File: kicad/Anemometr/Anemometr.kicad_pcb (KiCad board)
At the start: 2 copper layers, 44.9 x 48.9 mm, 158 parts, among them J1 Conn_01x01_Female, J10 +Z3, J11 -Z3, J12 +Z4, J13 -Z4, J14 SWD, J15 SWC, J16 Z4, J17 Z4, J18 1, J19 2, J2 Conn_01x01_Female, J20 3, J21 4, J22 5, J23 6, J24 7, J25 8, J26 Z4, J27 Z4, J28 Z4, J29 Z4, J3 RST, J30 Z4, J31 Z4, J32 Z4, J33 Z4, J34 Z4, J35 Z4, J4 TxD, J5 RxD, J6 +Z1, J7 -Z1, J8 +Z2, J9 -Z2, U1 TS5A3166DBVR, U10 MCP1700-3002E, U2 LMV7239, U3 TS5A3166DBVR, U4 TS5A3166DBVR, U5 STM32F103C8Tx, U6 TS5A3166DBVR, U7 LM2734Y, U8 MCP1700-5002E, U9 MCP1700-3002E, Y1 8MHz, Y2 25MHz

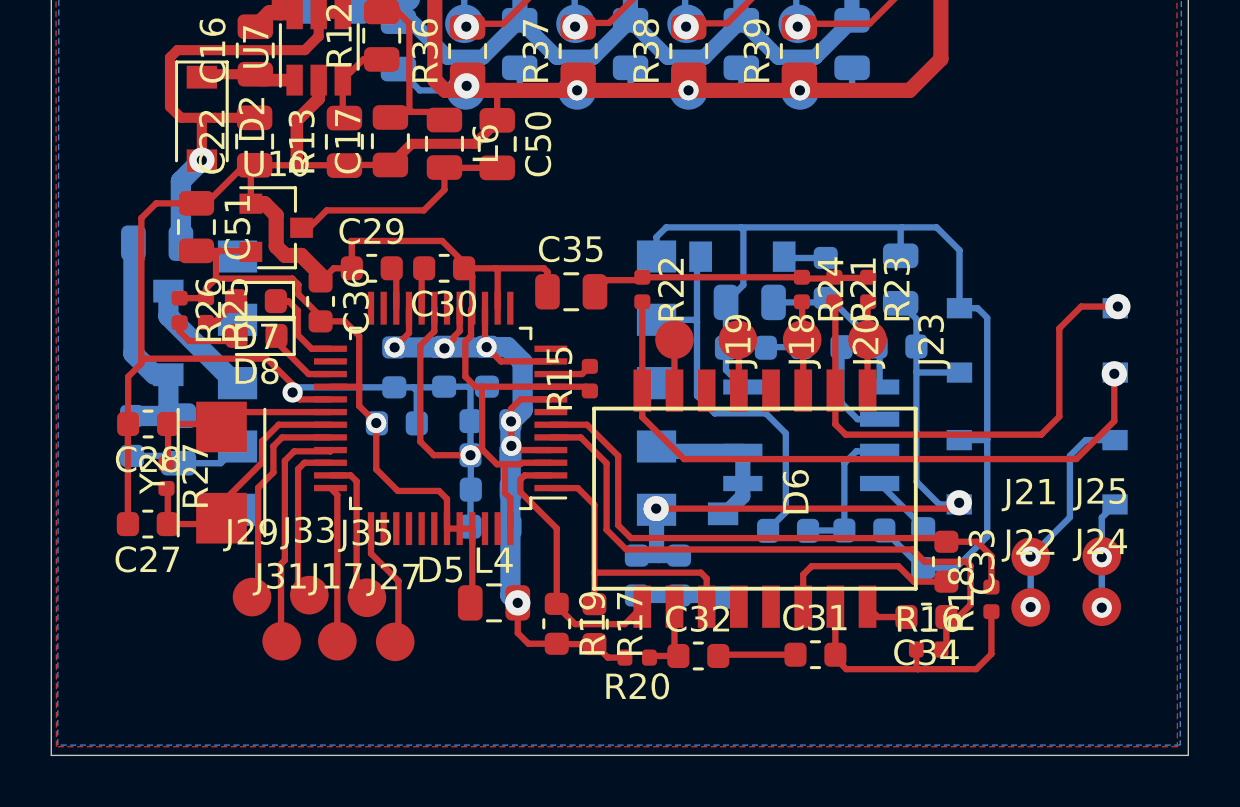
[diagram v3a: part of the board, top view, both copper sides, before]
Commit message: изменено:      kicad/Anemometr/Anemometr-cache.lib 	изменено:      kicad/Anemometr/Anemometr-rescue.lib 	изменено:      kicad/Anemometr/Anemometr.kicad_pcb 	изменено:      kicad/Anemometr/Anemometr.kicad_pcb-bak 	изменено:      kicad/Anemometr/Anemometr.sch 	изменено:      kicad/Anemometr/Anemometr.sch-bak 	изменено:      kicad/Anemometr/fp-info-cache
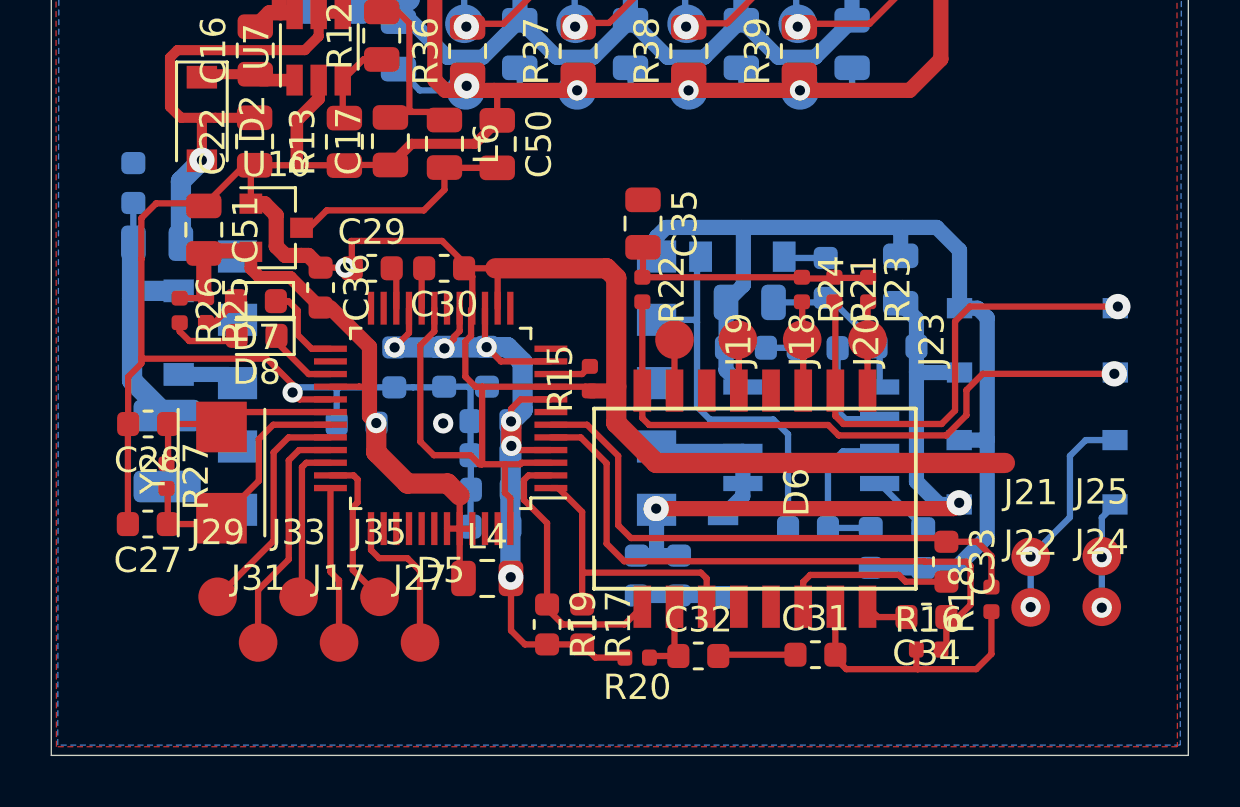
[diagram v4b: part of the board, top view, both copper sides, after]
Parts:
- C49: footprint Capacitor_SMD:C_0805_2012Metric -> Capacitor_SMD:C_1210_3225Metric
- C5: value 100nF -> 1.5nF
- J18: value 1 -> 1 TxD+
- J19: value 2 -> 2 TxD-
- J20: value 3 -> 3 RxD+
- J23: value 6 -> 6 RxD-
- R11: value 510 -> 3k
- R36, R37, R38, R39: value 10k -> 3k
- R4: value 100k -> 200k
- moved R35 9.98 mm to (22.1, 85.9), turned to 90 degrees
- moved C35 3.91 mm to (42.2, 87.5), turned to 270 degrees
- moved C37 1.59 mm to (30.9, 95.4), turned to 0 degrees
- moved J29 1.36 mm to (25.4, 102.2)
- moved L4 1.00 mm to (36.1, 101.5)
- moved J27 0.98 mm to (33.4, 104.1)
- moved J31 0.93 mm to (27.0, 104.1)
- moved R29 0.80 mm to (48.7, 99.5)
- moved R30 0.73 mm to (51.2, 100.3), turned to 270 degrees
- moved C49 0.64 mm to (23.4, 96.5)
- moved C36 0.55 mm to (29.5, 90.0)
- moved J35 0.50 mm to (31.8, 102.2)
- moved R17 0.48 mm to (39.8, 103.3)
- moved J33 0.43 mm to (28.6, 102.2)
- moved D14 0.41 mm to (23.9, 91.8), turned to 270 degrees
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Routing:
- net GND: track 338.8 -> 358.9 mm, vias 13 -> 14
- net Net-(D14-Pad2): track 4.81 -> 2.46 mm
- net +3.3VDAC: track 27.3 -> 26.0 mm
- net Net-(D6-Pad15): track 26.2 -> 25.0 mm
- net Net-(C49-Pad1): track 9.70 -> 11.0 mm
- net Net-(C35-Pad2): track 11.1 -> 10.0 mm
- net Net-(D5-Pad37): track 4.97 -> 5.95 mm
- net Net-(D12-Pad3): track 5.68 -> 6.41 mm
- net Net-(D6-Pad10): track 20.3 -> 19.7 mm

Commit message: изменено:      kicad/Anemometr/Anemometr.kicad_pcb 	изменено:      kicad/Anemometr/Anemometr.kicad_pcb-bak 	изменено:      kicad/Anemometr/Anemometr.sch 	изменено:      kicad/Anemometr/Anemometr.sch-bak 	изменено:      kicad/Anemometr/fp-info-cache
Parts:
- C1, C2, C3, C4, C5, C6, C7, C8: footprint Capacitor_SMD:C_0805_2012Metric -> Capacitor_SMD:C_0603_1608Metric
- R10, R11, R2, R3, R36, R37, R38, R39, R4, R5, R6, R7, R8, R9: footprint Resistor_SMD:R_0805_2012Metric -> Resistor_SMD:R_0603_1608Metric
- moved J22 15.2 mm to (60.6, 87.7)
- moved J21 15.2 mm to (60.6, 85.8)
- moved J24 15.1 mm to (58.1, 87.7)
- moved J25 15.0 mm to (58.1, 85.8)
- moved C35 11.8 mm to (54.0, 87.6), turned to 180 degrees
- moved R21 4.69 mm to (54.4, 90.9)
- moved R16 3.23 mm to (53.7, 101.1)
- moved C32 3.23 mm to (44.7, 101.4)
- moved D6 3.23 mm to (46.9, 95.1)
- moved C31 3.23 mm to (49.3, 101.3)
- moved J18 3.23 mm to (46.2, 88.9)
- moved J19 3.23 mm to (43.7, 88.9)
- moved R20 3.23 mm to (42.2, 101.4)
- moved C34 3.23 mm to (53.7, 99.8)
- moved J20 3.23 mm to (48.8, 88.9)
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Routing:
- net GND: track 358.9 -> 325.5 mm
- net Net-(D10-Pad2): track 4.29 -> 13.9 mm, vias 2 -> 1
- net Net-(D6-Pad10): track 19.7 -> 14.4 mm
- net Net-(C35-Pad2): track 10.0 -> 15.2 mm
- net Net-(C45-Pad1): track 26.8 -> 30.0 mm
- net +3.3VA: track 34.2 -> 31.6 mm
- net Net-(D10-Pad1): track 8.65 -> 11.2 mm, vias 2 -> 1
- net Net-(D5-Pad2): track 10.9 -> 8.51 mm
- net Net-(D5-Pad1): track 11.4 -> 9.13 mm
- net Net-(C31-Pad2): track 11.1 -> 8.82 mm
- net Net-(D5-Pad36): track 6.24 -> 4.00 mm
- net Net-(D6-Pad15): track 25.0 -> 22.9 mm
- net Net-(C34-Pad1): track 24.6 -> 22.5 mm
- net Net-(D5-Pad32): track 9.11 -> 10.9 mm
- net Net-(D5-Pad37): track 5.95 -> 4.29 mm
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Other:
- board size 44.9 x 48.9 mm -> 44.9 x 45.2 mm

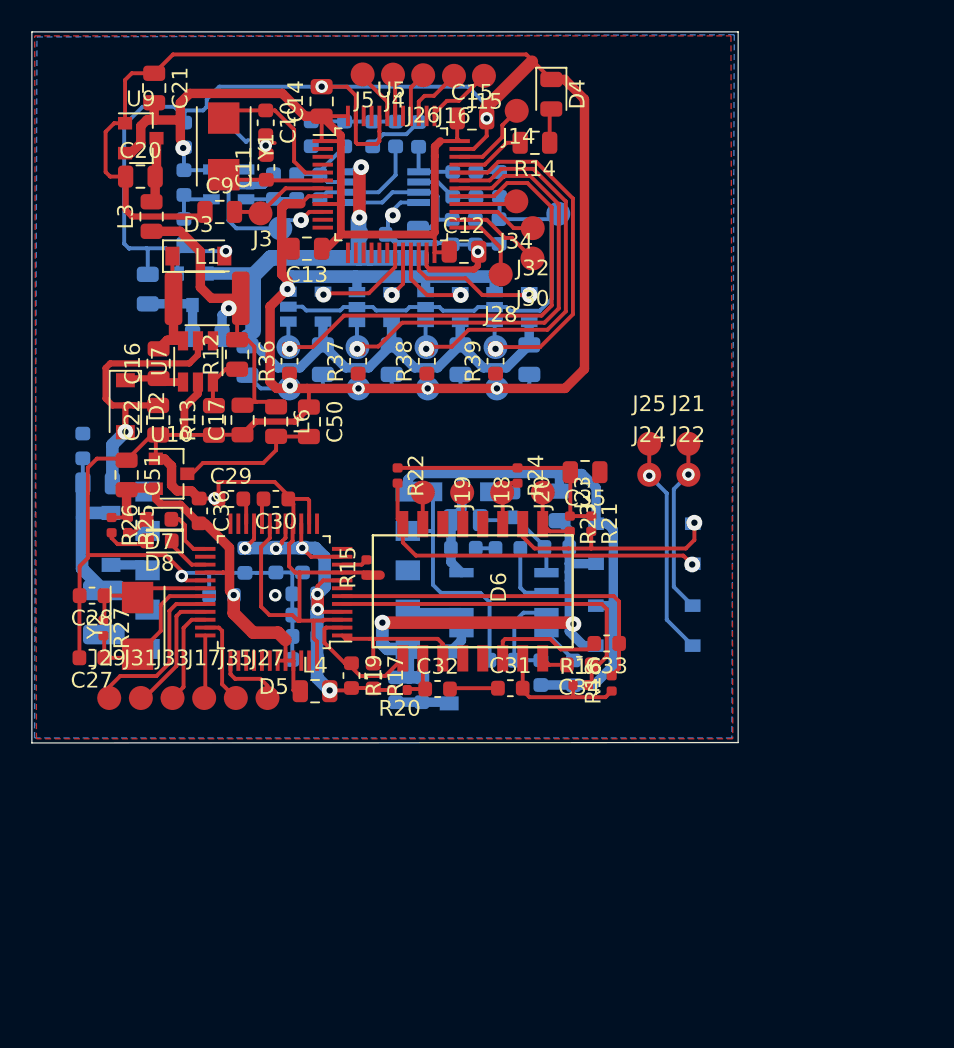
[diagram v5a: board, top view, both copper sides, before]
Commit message: изменено:      kicad/Anemometr/Anemometr.kicad_pcb 	изменено:      kicad/Anemometr/Anemometr.kicad_pcb-bak 	изменено:      kicad/Anemometr/Anemometr.sch 	изменено:      kicad/Anemometr/Anemometr.sch-bak
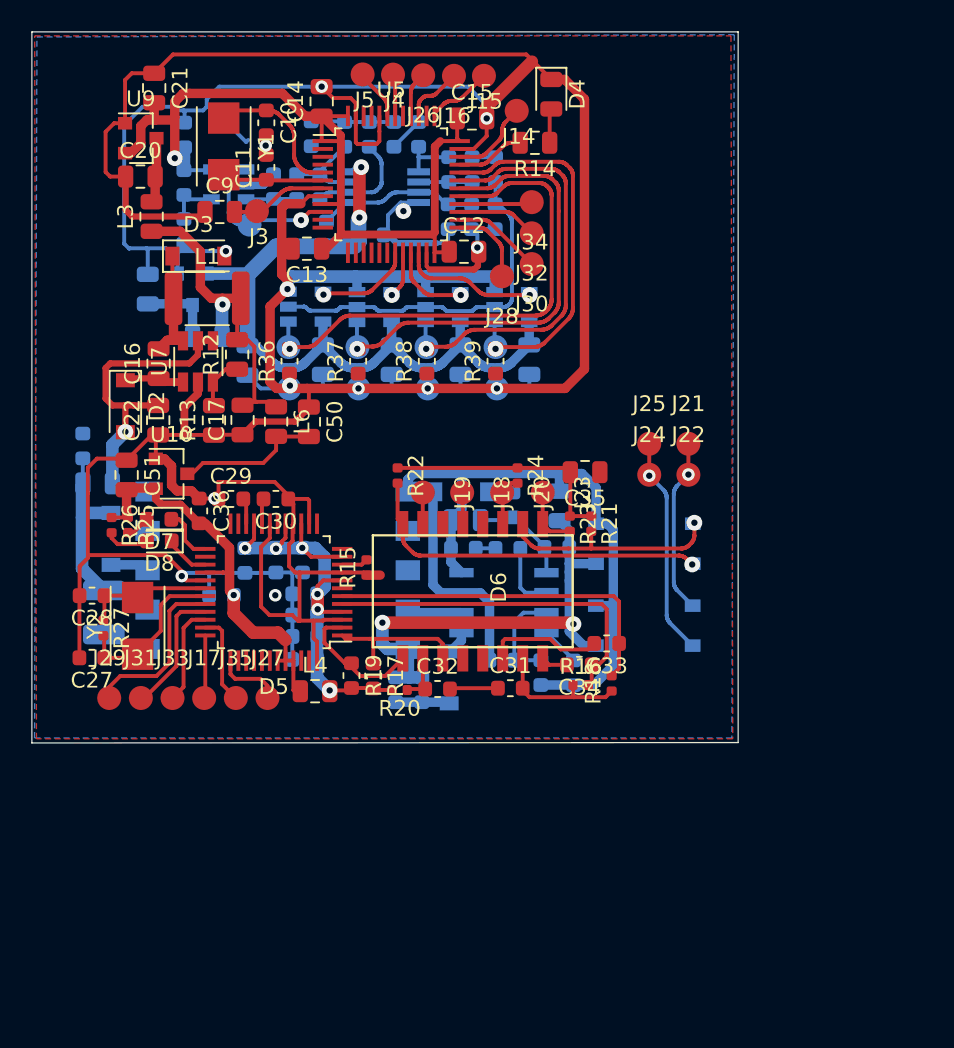
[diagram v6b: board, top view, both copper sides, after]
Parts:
- removed J1: Conn_01x01_Female, My-library:SMD-CONN
- R1: footprint Resistor_SMD:R_0805_2012Metric -> Resistor_SMD:R_0603_1608Metric
- R15: value 10k -> 12.4k
- moved R1 5.85 mm to (37.6, 72.4)
- moved J2 1.97 mm to (32.7, 71.8)
- moved C7 1.67 mm to (40.3, 66.1)
- moved R6 1.35 mm to (41.9, 66.1)
- moved C8 1.01 mm to (45.3, 71.3)
- moved R8 1.01 mm to (46.8, 71.3)
- moved J34 0.98 mm to (50.6, 70.4)
- moved C4 0.97 mm to (48.3, 68.4)
- moved R4 0.97 mm to (45.4, 68.4)
- moved R7 0.97 mm to (48.3, 71.3)
- moved R5 0.97 mm to (46.9, 68.4)
- moved J30 0.36 mm to (50.6, 74.4)
- moved J32 0.34 mm to (50.6, 72.4)
- moved J3 0.27 mm to (33.2, 71.0)
- moved J28 0.14 mm to (48.7, 75.1)
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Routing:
- net Net-(C4-Pad2): track 28.6 -> 23.0 mm
- net +5VA: track 53.1 -> 48.5 mm
- net Net-(C6-Pad1): track 3.62 -> 2.22 mm
- net +3V3: track 54.7 -> 55.9 mm
- net Net-(C8-Pad2): track 11.3 -> 10.2 mm
- net Net-(J34-Pad1): track 3.54 -> 4.63 mm
- net GND: track 325.5 -> 326.5 mm
- net Net-(J12-Pad1): track 23.2 -> 24.0 mm
- net Net-(D1-Pad2): track 4.03 -> 3.40 mm
- net SensorInput: track 10.9 -> 10.3 mm
- net Net-(J10-Pad1): track 26.3 -> 26.9 mm
- net Net-(C17-Pad2): track 21.8 -> 21.2 mm

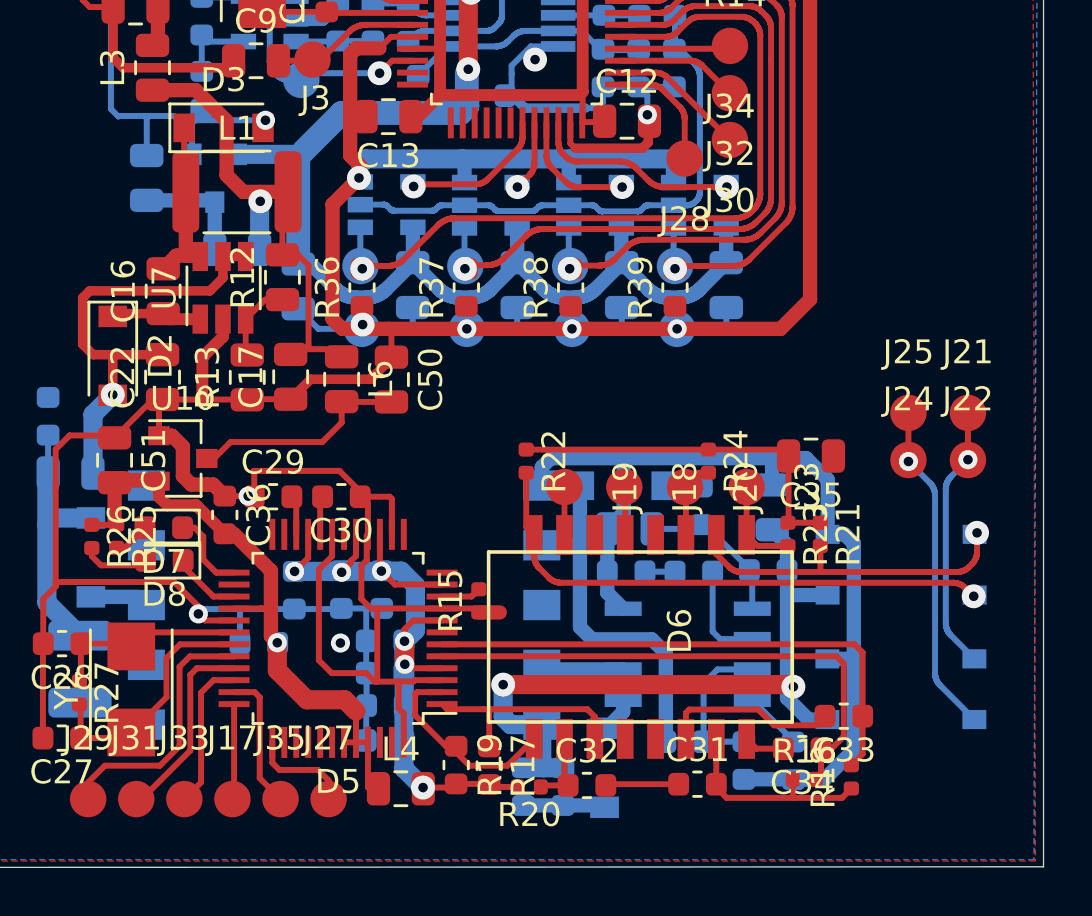
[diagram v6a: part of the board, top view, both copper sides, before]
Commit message: изменено:      kicad/Anemometr/Anemometr-cache.lib 	изменено:      kicad/Anemometr/Anemometr.kicad_pcb 	изменено:      kicad/Anemometr/Anemometr.kicad_pcb-bak 	изменено:      kicad/Anemometr/Anemometr.sch 	изменено:      kicad/Anemometr/Anemometr.sch-bak 	изменено:      kicad/Anemometr/fp-info-cache
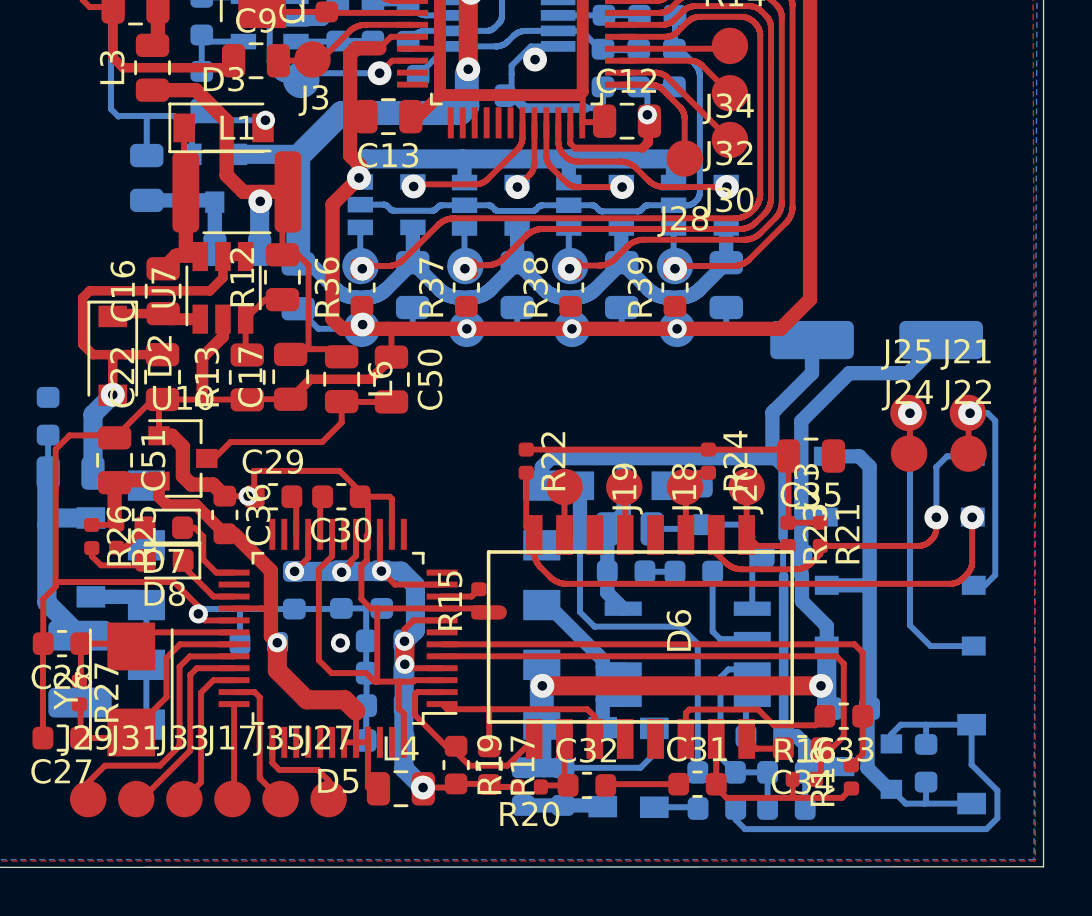
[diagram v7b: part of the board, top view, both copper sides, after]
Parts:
- added C52: 28p, Capacitor_SMD:C_0603_1608Metric, B.Cu at (53.0, 102.3)
- added D16: MM1Z27, Diode_SMD:D_SOD-123, B.Cu at (47.5, 100.6)
- added D17: BZT52-C15, Diode_SMD:D_SOD-123, B.Cu at (60.7, 100.5)
- added Q1: 5N10, Package_TO_SOT_SMD:SOT-23, B.Cu at (56.4, 100.6)
- added R40: 51k, Resistor_SMD:R_0603_1608Metric, B.Cu at (50.1, 102.3)
- added R41: 24k, Resistor_SMD:R_0603_1608Metric, B.Cu at (55.7, 98.1)
- added R42: 237k, Resistor_SMD:R_0603_1608Metric, B.Cu at (58.8, 100.4)
- C45: value 10uF/100v -> 22uF/63v; footprint Capacitor_SMD:C_0805_2012Metric -> Capacitor_SMD:CP_Elec_6.3x7.7
- C47: value 6.8nF -> 480p
- C48: value 6.8nF -> 10nF
- D15: value DA2257 -> T4932B
- R28: value 150R -> 100k
- R29: value 150R -> 43k
- R30, R34: value 150R -> 10k
- R31: value 150R -> 20R
- R32: value 150R -> 47R
- R33: value 150R -> R68
- moved C45 8.25 mm to (56.8, 82.7), turned to 180 degrees
- moved D9 3.26 mm to (57.7, 88.9)
- moved D10 3.07 mm to (57.8, 94.3)
- moved R29 1.85 mm to (50.1, 100.8)
- moved R30 1.85 mm to (53.0, 100.8), turned to 0 degrees
- moved R33 1.58 mm to (52.1, 99.3), turned to 0 degrees
- moved R28 0.87 mm to (52.9, 91.8)
- moved J22 0.27 mm to (60.6, 87.5)
- moved J24 0.27 mm to (58.1, 87.5)
- moved D13 0.08 mm to (45.3, 100.6)
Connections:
- D10 pad 4: Net-(C45-Pad2) -> Net-(D10-Pad4)
- D15 pad 10: (no net) -> GND
- D15 pad 3: (no net) -> Net-(D12-Pad5)
- D15 pad 4: Net-(D12-Pad5) -> Net-(C45-Pad1)
- D15 pad 6: (no net) -> Net-(D14-Pad2)
- D15 pad 7: GND -> Net-(D14-Pad2)
- D15 pad 9: (no net) -> GND
- D9 pad 4: Net-(C45-Pad2) -> Net-(D10-Pad4)
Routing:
- net Net-(D10-Pad4): track 0.00 -> 22.4 mm
- net Net-(D17-Pad1): track 0.00 -> 20.9 mm
- net Net-(C45-Pad1): track 30.0 -> 43.7 mm
- net Net-(D14-Pad2): track 2.46 -> 7.46 mm
- net Net-(D11-Pad2): track 15.4 -> 17.8 mm
- net Net-(C52-Pad1): track 6.41 -> 8.67 mm
- net Net-(D6-Pad15): track 22.8 -> 24.8 mm
- net Net-(D16-Pad2): track 0.00 -> 1.85 mm
- net Net-(C46-Pad1): track 6.47 -> 8.28 mm
- net Net-(D12-Pad5): track 6.36 -> 8.10 mm
- net Net-(D6-Pad10): track 14.3 -> 15.3 mm
- net Net-(D12-Pad4): track 2.48 -> 1.63 mm
- net Net-(D10-Pad1): track 11.1 -> 10.4 mm

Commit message: изменено:      kicad/Anemometr/Anemometr.kicad_pcb 	изменено:      kicad/Anemometr/Anemometr.kicad_pcb-bak 	изменено:      kicad/Anemometr/Anemometr.sch 	изменено:      kicad/Anemometr/Anemometr.sch-bak 	изменено:      kicad/Anemometr/fp-info-cache
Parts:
- removed R22: 75R, Resistor_SMD:R_0402_1005Metric
- added D18: LED, LED_SMD:LED_0603_1608Metric, B.Cu at (23.5, 82.2)
- added D19: LED, LED_SMD:LED_0603_1608Metric, B.Cu at (30.2, 82.0)
- added J1: +5.5v, My-library:SMD-CONN, F.Cu at (24.6, 73.4)
- added R43: 4.7k, Resistor_SMD:R_0603_1608Metric, B.Cu at (23.5, 83.6)
- added R44: 2k, Resistor_SMD:R_0603_1608Metric, B.Cu at (30.2, 80.6)
- C37, C43: moved to F.Cu
- C49: value 20uF -> 220uF; footprint Capacitor_SMD:C_1210_3225Metric -> Capacitor_Tantalum_SMD:CP_EIA-7343-15_Kemet-W
- moved C48 15.9 mm to (43.2, 85.5), turned to 0 degrees
- moved R34 14.4 mm to (43.2, 87.1), turned to 0 degrees
- moved D16 13.8 mm to (50.2, 87.0)
- moved R40 13.8 mm to (52.5, 88.7)
- moved D11 13.6 mm to (47.9, 102.3)
- moved D13 13.4 mm to (45.9, 87.2), turned to 270 degrees
- moved R30 11.0 mm to (42.0, 101.1), turned to 270 degrees
- moved Q1 10.7 mm to (51.2, 91.2)
- moved R42 10.7 mm to (53.6, 91.1)
- moved R31 10.1 mm to (50.8, 99.6), turned to 90 degrees
- moved D17 9.60 mm to (52.7, 95.2), turned to 90 degrees
- moved R28 7.89 mm to (52.3, 99.6), turned to 90 degrees
- moved C37 7.49 mm to (34.4, 102.0), turned to 90 degrees
- moved C47 7.37 mm to (47.8, 99.6), turned to 270 degrees
- moved R33 7.36 mm to (44.7, 99.6), turned to 270 degrees
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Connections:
- D17 pad 1: Net-(D17-Pad1) -> Net-(D10-Pad4)
- D17 pad 2: Net-(D10-Pad4) -> Net-(D17-Pad2)
- Q1 pad 1: Net-(D17-Pad1) -> Net-(D17-Pad2)
- R23 pad 2: Net-(D6-Pad9) -> Net-(D6-Pad11)
- R24 pad 2: Net-(D6-Pad11) -> Net-(D6-Pad9)
- R40 pad 1: Net-(D17-Pad1) -> Net-(D17-Pad2)
- R42 pad 1: Net-(D17-Pad1) -> Net-(D17-Pad2)
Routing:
- net GND: track 326.5 -> 303.5 mm, vias 14 -> 15
- net Net-(D17-Pad1): track 20.9 -> 0.00 mm
- net Net-(D10-Pad4): track 22.4 -> 12.0 mm
- net Net-(C35-Pad2): track 15.2 -> 6.60 mm
- net Net-(D17-Pad2): track 0.00 -> 8.02 mm
- net Net-(C45-Pad1): track 43.7 -> 49.3 mm, vias 2 -> 0
- net Net-(D10-Pad1): track 10.4 -> 14.5 mm
- net Net-(D10-Pad2): track 13.6 -> 17.5 mm
- net Net-(C17-Pad2): track 21.2 -> 24.7 mm
- net Net-(D6-Pad15): track 24.8 -> 21.3 mm
- net Net-(C45-Pad2): track 40.3 -> 37.1 mm
- net Net-(D11-Pad2): track 17.8 -> 14.9 mm
- net Net-(J12-Pad1): track 24.0 -> 26.7 mm
- net Net-(J10-Pad1): track 26.9 -> 29.4 mm
- net Net-(J8-Pad1): track 29.8 -> 32.3 mm
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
